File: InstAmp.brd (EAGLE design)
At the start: 41.3 x 18 mm, 35 parts, among them IC1 AD8221ARZ, IC2 TLC2254ID

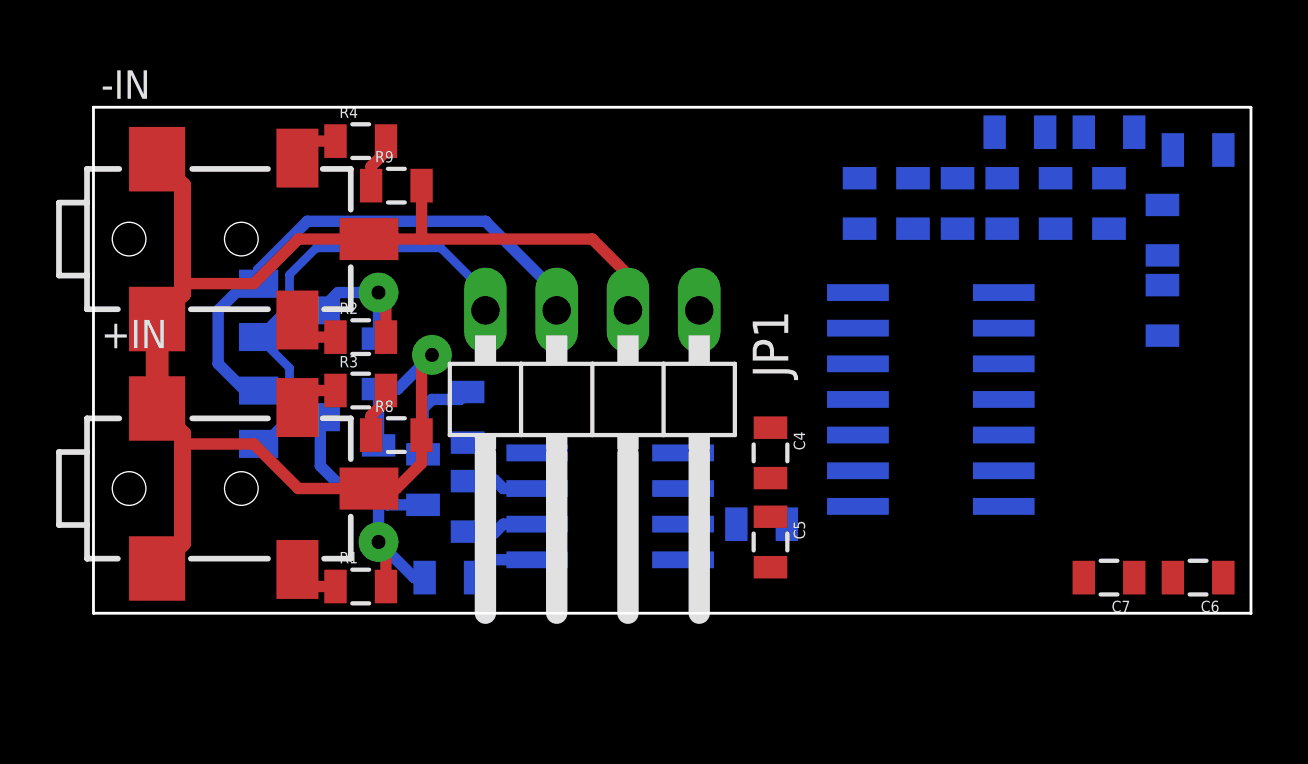
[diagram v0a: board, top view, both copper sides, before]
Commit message: Dimension correction
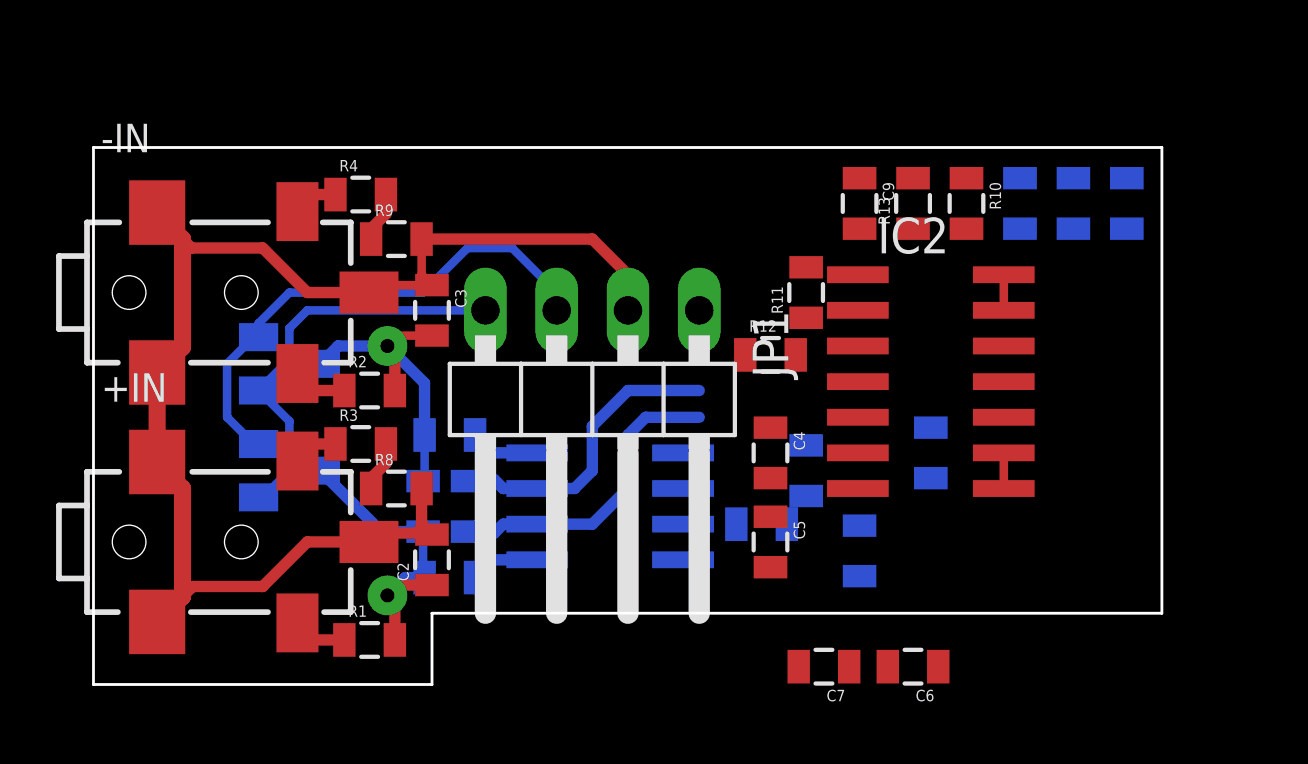
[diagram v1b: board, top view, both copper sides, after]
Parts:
- moved R15 15.7 mm to (27.3, 2.22), turned to 90 degrees
- moved C11 14.4 mm to (29.8, 5.71), turned to 90 degrees
- moved R16 13.9 mm to (25.4, 5.08), turned to 270 degrees
- moved C7 10.6 mm to (26.0, -1.91)
- moved C6 10.6 mm to (29.2, -1.91)
- moved R12 8.58 mm to (24.1, 9.21), flipped to the top, turned to 0 degrees
- moved R13 7.43 mm to (29.2, 14.6), flipped to the top, turned to 90 degrees
- moved R11 4.96 mm to (25.4, 11.4), flipped to the top
- moved C2 3.70 mm to (12.1, 1.91), flipped to the top
- moved R10 3.18 mm to (31.1, 14.6), flipped to the top, turned to 270 degrees
- moved C3 2.69 mm to (12.1, 10.8), flipped to the top, turned to 270 degrees
- moved R1 1.93 mm to (9.84, -0.95)
- moved R2 1.93 mm to (9.84, 7.94)
- moved -IN 1.91 mm to (1.27, 11.4)
- moved R4 1.91 mm to (9.53, 14.9)
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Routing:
- net N$16: track 2.63 -> 11.1 mm
- net N$8: track 2.63 -> 10.8 mm
- net GND: track 55.3 -> 48.8 mm, vias 1 -> 0
- net N$13: track 0.00 -> 2.48 mm
- net N$5: track 9.14 -> 11.5 mm
- net -5V: track 16.2 -> 14.7 mm
- net N$17: track 1.81 -> 3.08 mm
- net N$7: track 1.81 -> 3.08 mm
- net +5V: track 19.1 -> 18.5 mm
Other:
- board size 41.3 x 18 mm -> 38.1 x 19.1 mm

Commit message: .
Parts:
- moved C5 13.2 mm to (18.1, 14.3), flipped to the bottom, turned to 0 degrees
- moved R13 11.5 mm to (30.5, 3.17), flipped to the bottom, turned to 180 degrees
- moved C7 11.4 mm to (35.6, 4.45)
- moved C4 9.09 mm to (15.9, 9.53), flipped to the bottom, turned to 180 degrees
- moved C6 7.75 mm to (35.6, 2.54), turned to 0 degrees
- moved R10 5.41 mm to (25.7, 14.3), flipped to the bottom, turned to 180 degrees
- moved R17 5.41 mm to (31.4, 14.3), turned to 90 degrees
- moved R14 5.09 mm to (29.8, 14.3), turned to 90 degrees
- moved C11 5.02 mm to (27.0, 1.59), turned to 180 degrees
- moved C8 4.77 mm to (28.3, 14.3), turned to 270 degrees
- moved C9 4.77 mm to (22.5, 14.3), flipped to the bottom, turned to 0 degrees
- moved JP1 1.42 mm to (18.4, 8.26)
- moved R15 1.00 mm to (27.0, 3.17), turned to 180 degrees
- moved R16 0.63 mm to (24.8, 5.08), flipped to the top
- moved R11 0.32 mm to (25.1, 11.4)
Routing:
- net N$17: track 3.08 -> 32.0 mm
- net N$7: track 3.08 -> 28.4 mm
- net N$8: track 10.8 -> 26.6 mm, vias 0 -> 1
- net N$16: track 11.1 -> 26.3 mm, vias 0 -> 1
- net GND: track 48.8 -> 56.9 mm
- net -5V: track 14.7 -> 18.6 mm
- net +5V: track 18.5 -> 21.6 mm

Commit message: Amp routing
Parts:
- moved R13 11.3 mm to (28.3, 14.3), flipped to the top, turned to 90 degrees
- moved R12 10.7 mm to (34.6, 11.4), turned to 180 degrees
- moved R16 10.1 mm to (34.6, 2.86)
- moved R11 9.78 mm to (34.6, 13.7)
- moved R17 9.74 mm to (34.6, 5.08), flipped to the top, turned to 180 degrees
- moved C7 9.67 mm to (26.7, 8.26), flipped to the bottom, turned to 0 degrees
- moved R14 8.99 mm to (34.6, 6.67), flipped to the top, turned to 180 degrees
- moved C9 8.89 mm to (31.4, 14.3), flipped to the top, turned to 270 degrees
- moved C8 7.75 mm to (34.6, 9.84), flipped to the top, turned to 0 degrees
- moved C6 7.24 mm to (31.1, 8.26), flipped to the bottom
- moved R15 4.55 mm to (31.4, 2.22), flipped to the top, turned to 90 degrees
- moved R10 4.13 mm to (29.8, 14.3), flipped to the top, turned to 270 degrees
- moved C11 2.93 mm to (29.8, 2.22), flipped to the top, turned to 90 degrees
- moved IC2 0.63 mm to (29.2, 8.26), turned to 90 degrees
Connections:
- net N$10: now also IC2.2; no longer IC2.6
- net N$14: now also IC2.5; no longer IC2.3
- net N$16: now also IC2.12; no longer IC2.10
- net N$17: now also IC2.13, IC2.14; no longer IC2.8, IC2.9
- net N$22: now also IC2.3; no longer IC2.5
- net N$23: now also IC2.6; no longer IC2.2
- net N$7: now also IC2.8, IC2.9; no longer IC2.13, IC2.14
- net N$8: now also IC2.10; no longer IC2.12
- net N$9: now also IC2.1; no longer IC2.7
- net OUT: now also IC2.7; no longer IC2.1
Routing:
- net +5V: track 21.6 -> 45.6 mm, vias 0 -> 1
- net -5V: track 18.6 -> 42.1 mm, vias 0 -> 1
- net GND: track 56.9 -> 74.8 mm
- net OUT: track 0.00 -> 14.7 mm, vias 0 -> 1
- net N$9: track 0.00 -> 11.2 mm
- net N$16: track 26.3 -> 16.1 mm
- net N$8: track 26.6 -> 17.4 mm
- net N$7: track 28.4 -> 21.9 mm
- net N$17: track 32.0 -> 25.5 mm
- net N$14: track 0.00 -> 5.46 mm
- net N$15: track 0.00 -> 3.18 mm
- net N$11: track 0.00 -> 1.90 mm
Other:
- board size 38.1 x 19.1 mm -> 37.4 x 19.1 mm

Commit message: Amp routing
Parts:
- moved C5 11.7 mm to (24.4, 4.45), flipped to the top, turned to 270 degrees
- moved C11 5.75 mm to (35.6, 2.86)
- moved R11 2.03 mm to (33.0, 14.9), turned to 180 degrees
- moved R15 0.90 mm to (30.8, 2.86), turned to 0 degrees
- moved C10 0.71 mm to (24.4, 3.49)
- moved R16 0.64 mm to (34.0, 2.86)
- moved C9 0.64 mm to (30.8, 14.3)
- moved R13 0.64 mm to (27.6, 14.3)
- moved R10 0.63 mm to (29.2, 14.3)
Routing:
- net GND: track 74.8 -> 119.8 mm, vias 0 -> 1
- net +5V: track 45.6 -> 62.9 mm, vias 1 -> 2
- net N$20: track 0.00 -> 12.5 mm, vias 0 -> 1
- net N$22: track 0.00 -> 6.05 mm
- net N$23: track 0.00 -> 5.74 mm
- net N$9: track 11.2 -> 15.7 mm
- net -5V: track 42.1 -> 46.5 mm
- net N$10: track 0.00 -> 3.59 mm
- net N$14: track 5.46 -> 7.75 mm
- net N$17: track 25.5 -> 26.5 mm
- net OUT: track 14.7 -> 15.5 mm
- net N$11: track 1.90 -> 2.66 mm
- net N$7: track 21.9 -> 21.2 mm

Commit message: Amp routing
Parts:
- moved C5 1.59 mm to (23.5, 3.17), flipped to the bottom
- moved C10 1.31 mm to (25.7, 3.17)
- moved R16 0.95 mm to (33.0, 2.86), turned to 180 degrees
- moved D1 0.63 mm to (7.62, 5.08)
- moved D2 0.63 mm to (7.62, 8.89)
- moved R15 0.63 mm to (30.2, 2.86)
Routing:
- net GND: track 119.8 -> 102.0 mm
- net +5V: track 62.9 -> 70.9 mm, vias 2 -> 1
- net N$20: track 12.5 -> 10.2 mm
- net N$9: track 15.7 -> 14.2 mm
- net N$11: track 2.66 -> 3.80 mm
- net -5V: track 46.5 -> 45.4 mm
- net N$10: track 3.59 -> 4.47 mm
- net N$6: track 11.2 -> 10.6 mm
- net N$5: track 11.5 -> 10.8 mm

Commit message: Polygons
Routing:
- net GND: track 102.0 -> 90.0 mm
- net N$17: track 26.2 -> 24.3 mm
- net +5V: track 70.9 -> 72.4 mm
- added copper zone on layer 16, net +5V
- added copper zone on layer 1, net GND
- added copper zone on layer 16, net GND

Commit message: .
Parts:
- moved C4 8.41 mm to (23.0, 5.08), turned to 270 degrees
- moved C5 1.00 mm to (23.8, 2.22)
- moved C10 0.95 mm to (26.7, 3.17)
- moved R15 0.90 mm to (30.8, 2.22), turned to 90 degrees
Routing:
- net -5V: track 45.1 -> 42.7 mm
- net GND: track 90.0 -> 87.9 mm
- net N$11: track 3.80 -> 5.54 mm
- net N$20: track 10.2 -> 9.02 mm
